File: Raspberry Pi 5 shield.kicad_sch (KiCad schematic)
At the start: 18 parts, among them J1 Raspberry Connector, J2 Conn_02x02_Odd_Even, U1 MCP2515-xSO

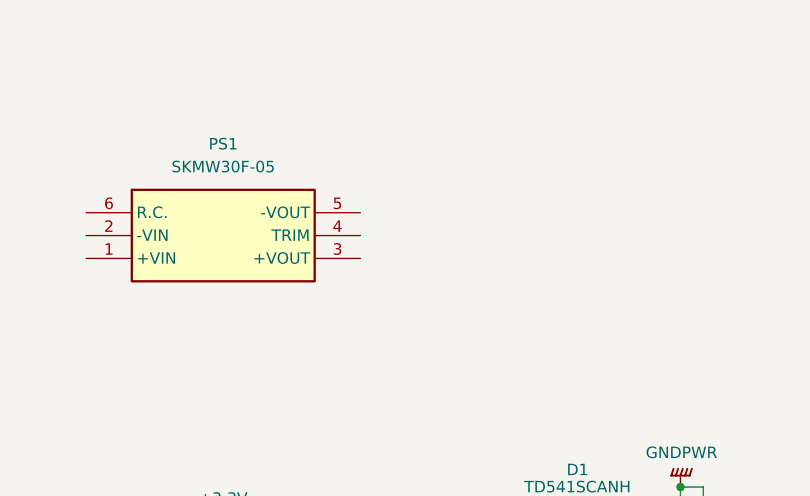
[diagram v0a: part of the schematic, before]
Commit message: Добавил подстроечный резистор к источнику питания
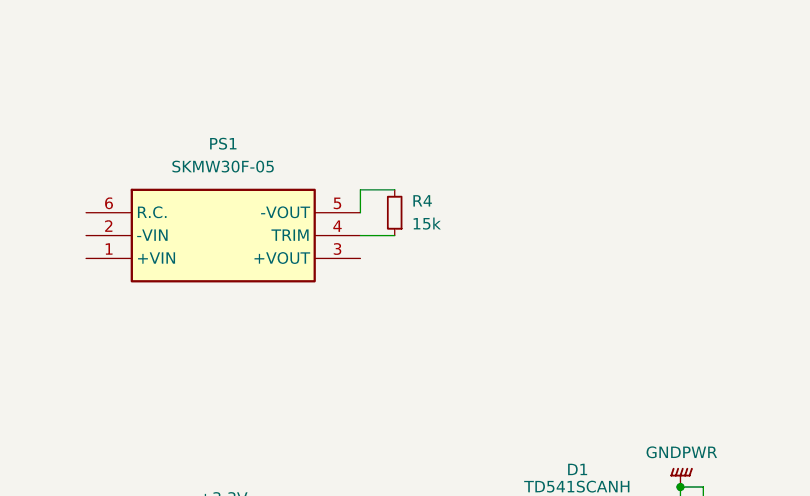
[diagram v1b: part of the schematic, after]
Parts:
- added R4: 15k, Resistor_SMD:R_0805_2012Metric_Pad1.20x1.40mm_HandSolder, symbol Device:R_Small
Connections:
- net at PS1.4 (TRIM): now also R4.1
- net at PS1.5 (-VOUT): now also R4.2
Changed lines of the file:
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@@
 	(wire
 		(pts
+			(xy 154.94 45.72) (xy 158.75 45.72)
+		)
+		(stroke
+			(width 0)
+			(type default)
+		)
+	)
+	(wire
+		(pts
 			(xy 189.23 85.09) (xy 202.565 85.09)
 		)
@@
 	(wire
 		(pts
+			(xy 154.94 40.64) (xy 158.75 40.64)
+		)
+		(stroke
+			(width 0)
+			(type default)
+		)
+	)
+	(wire
+		(pts
 			(xy 190.5 77.47) (xy 190.5 73.66)
 		)
@@
 	(wire
 		(pts
+			(xy 154.94 43.18) (xy 154.94 40.64)
+		)
+		(stroke
+			(width 0)
+			(type default)
+		)
+	)
+	(wire
+		(pts
 			(xy 154.94 85.09) (xy 168.91 85.09)
 		)
@@
 					(unit 1)
 				)
+			)
+		)
+	)
+	(symbol
+		(lib_id "Device:R_Small")
+		(at 158.75 43.18 180)
+		(unit 1)
+		(exclude_from_sim no)
+		(in_bom yes)
+		(on_board yes)
+		(dnp no)
+		(fields_autoplaced yes)
+		(property "Reference" "R4"
+			(at 160.655 41.91 0)
+			(effects
+				(font
+					(size 1.27 1.27)
+				)
+				(justify right)
+			)
+		)
+		(property "Value" "15k"
+			(at 160.655 44.45 0)
+			(effects
+				(font
+					(size 1.27 1.27)
+				)
+				(justify right)
+			)
+		)
+		(property "Footprint" "Resistor_SMD:R_0805_2012Metric_Pad1.20x1.40mm_HandSolder"
+			(at 158.75 43.18 0)
+			(effects
+				(font
+					(size 1.27 1.27)
+				)
+				(hide yes)
+			)
+		)
+		(property "Datasheet" "~"
+			(at 158.75 43.18 0)
+			(effects
+				(font
+					(size 1.27 1.27)
+				)
+				(hide yes)
+			)
+		)
+		(property "Description" "Resistor, small symbol"
+			(at 158.75 43.18 0)
+			(effects
+				(font
+					(size 1.27 1.27)
+				)
+				(hide yes)
+			)
+		)
+		(pin "2"
+		)
+		(pin "1"
+		)
+		(instances
+			(project "Raspberry Pi 5 shield"
+				(path "/2117c268-443a-419c-9380-190e5bd7137f"
+					(reference "R4")
+					(unit 1)
+				)

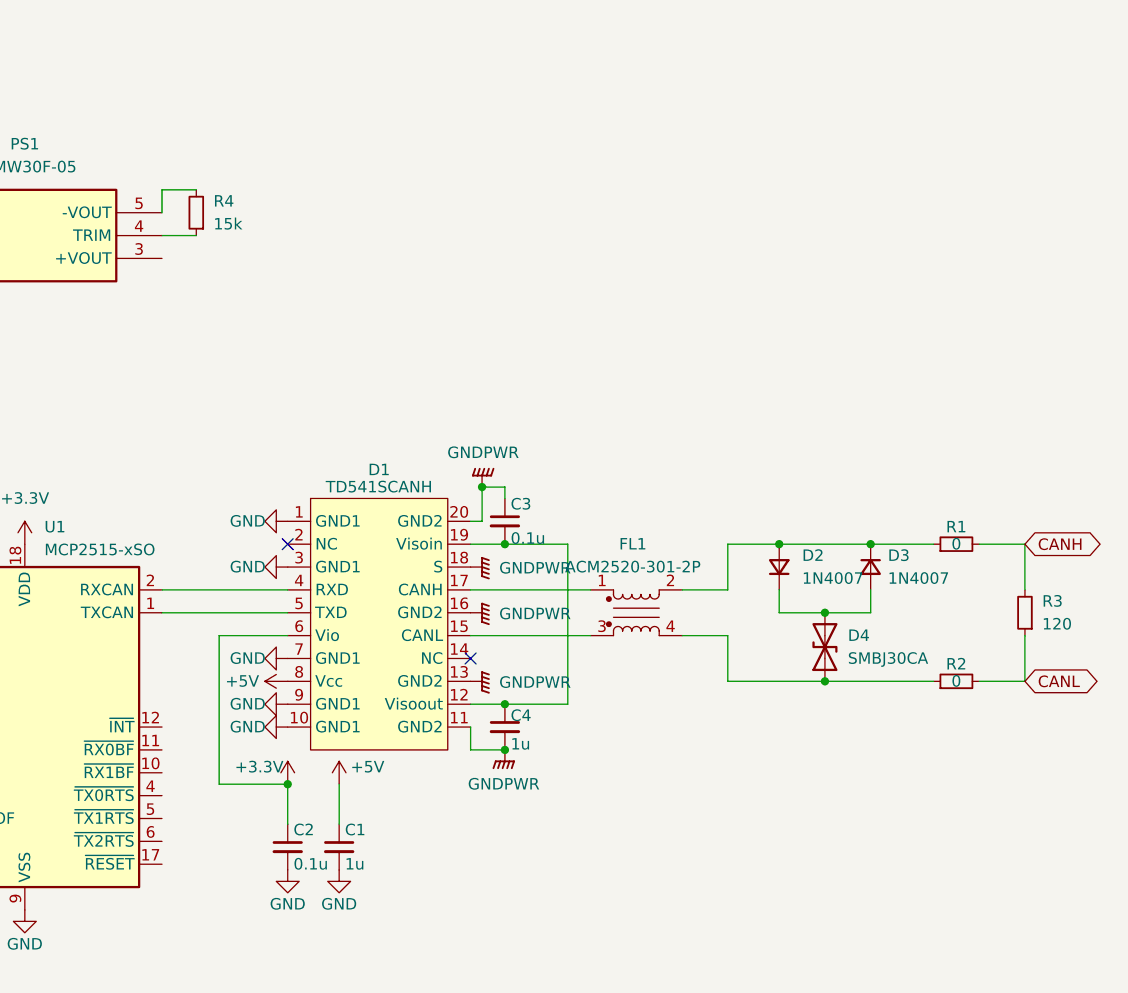
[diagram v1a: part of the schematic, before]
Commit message: Добавил конденсаторы по выходу
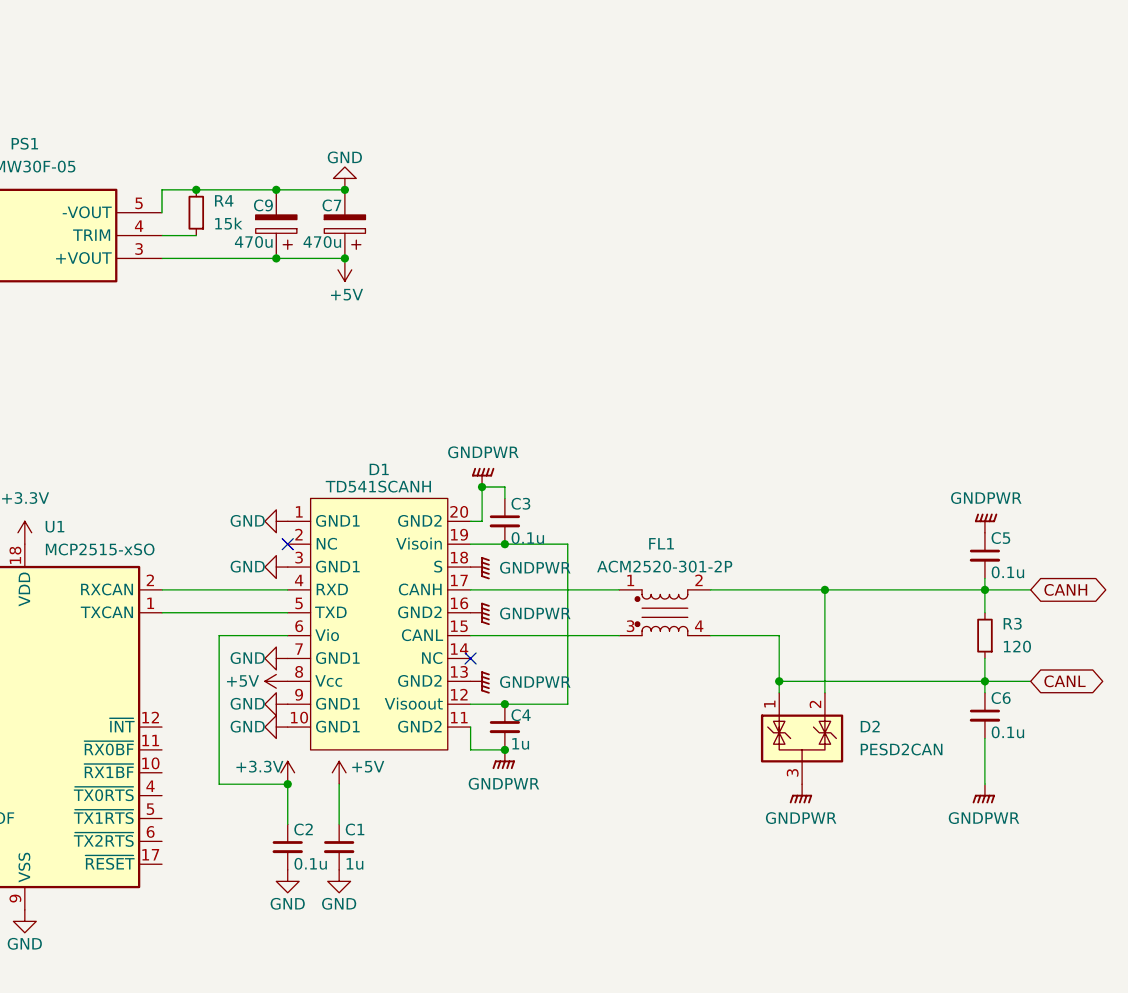
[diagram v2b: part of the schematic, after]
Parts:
- removed D2, D3: 1N4007, Diode_SMD:D_SMA_Handsoldering, symbol Device:D_Small
- removed D4: SMBJ30CA, Diode_SMD:D_SMB_Handsoldering, symbol Device:D_TVS
- removed R1, R2: 0, Resistor_SMD:R_0805_2012Metric_Pad1.20x1.40mm_HandSolder, symbol Device:R_Small
- added C5, C6: 0.1u, Capacitor_SMD:C_0805_2012Metric_Pad1.18x1.45mm_HandSolder, symbol Device:C_Small
- added C7, C9: 470u, Capacitor_SMD:CP_Elec_10x10, symbol Device:C_Polarized
- added D2: PESD2CAN, Package_TO_SOT_SMD:SOT-23, symbol Power_Protection:NUP2105L
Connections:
- net +5V: now also PS1.3 (+VOUT), C7.1, C9.1
- net CANH: now also FL1.2, C5.2, D2.2 (K)
- net CANL: now also FL1.4, C6.1, D2.1 (K)
- net GND: now also PS1.5 (-VOUT), R4.2, C7.2, C9.2
- net GNDPWR: now also C5.1, C6.2, D2.3 (A)
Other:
- moved on the sheet: FL1, R3

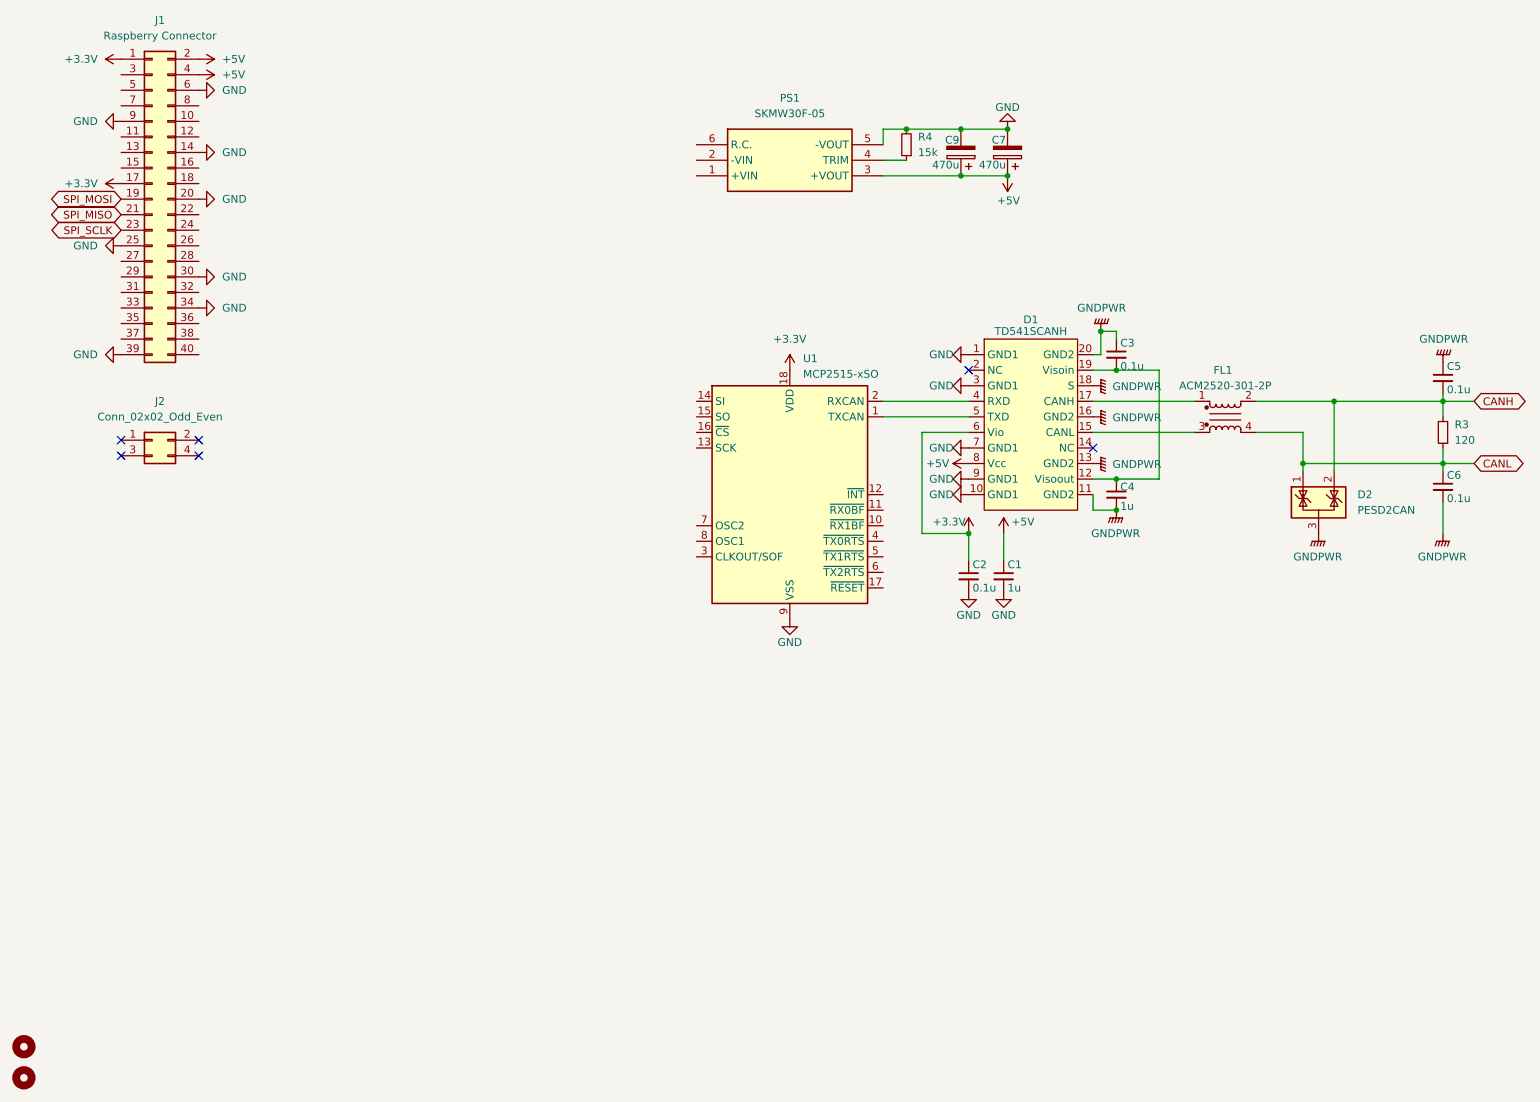
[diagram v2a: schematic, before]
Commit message: Добавил индикацию
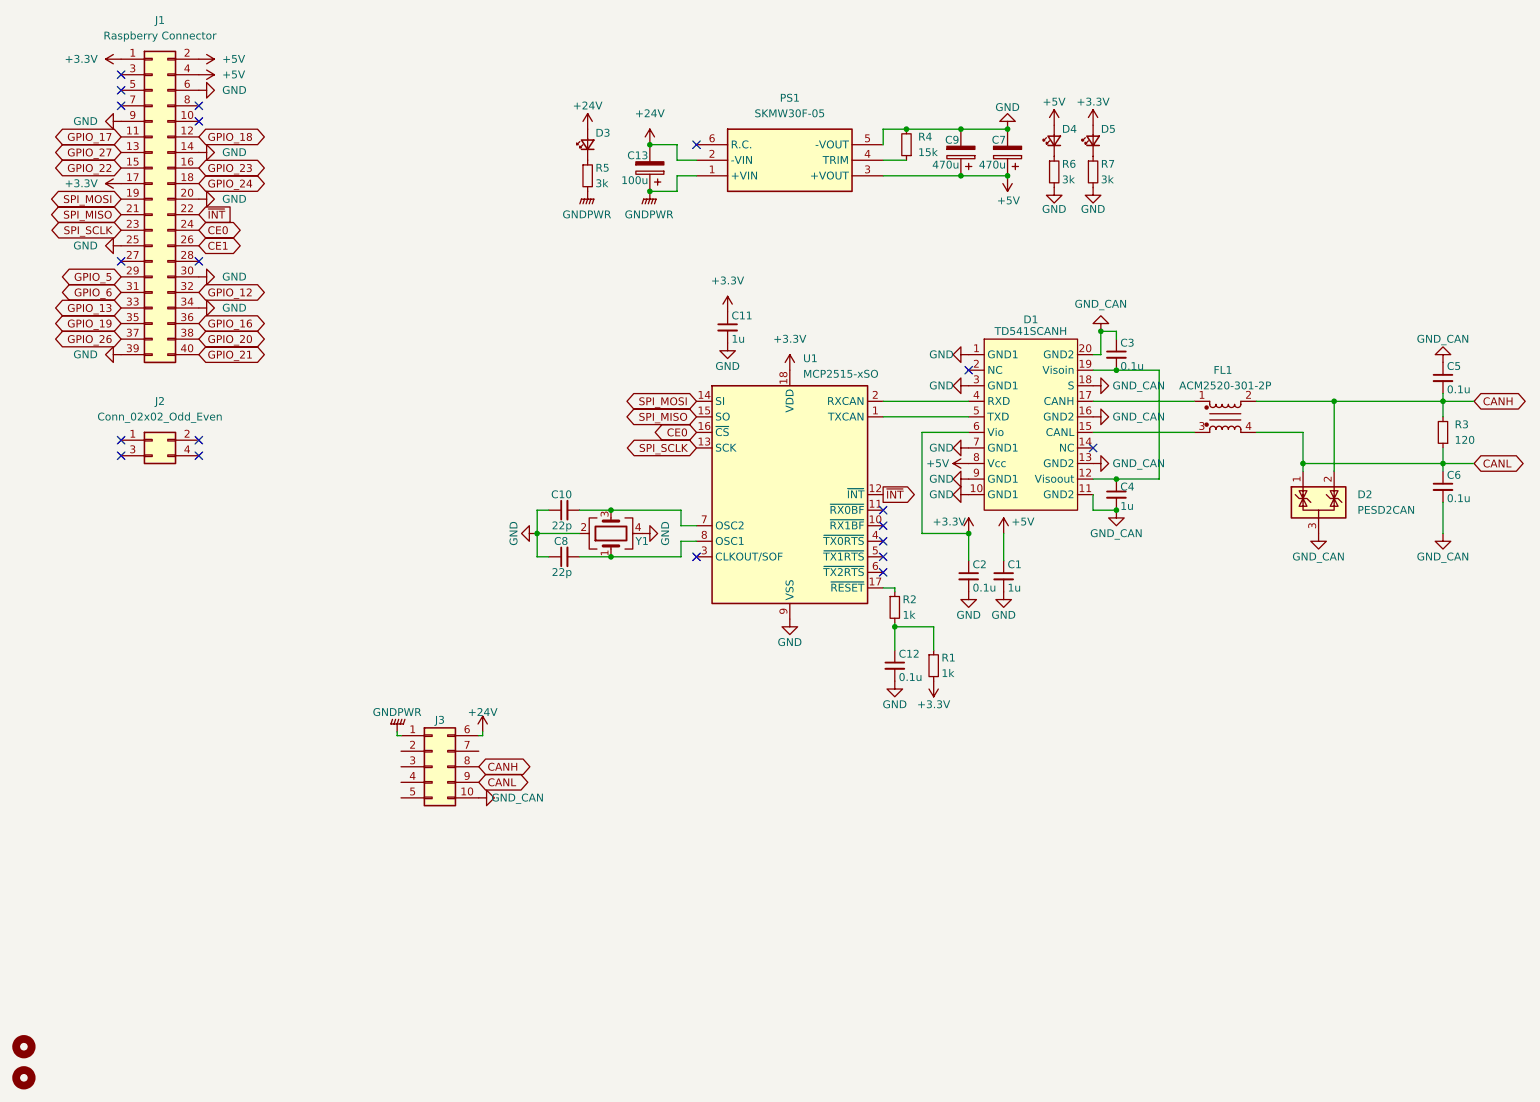
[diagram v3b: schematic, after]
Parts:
- added C10, C8: 22p, Capacitor_SMD:C_0805_2012Metric_Pad1.18x1.45mm_HandSolder, symbol Device:C_Small
- added C11: 1u, Capacitor_SMD:C_0805_2012Metric_Pad1.18x1.45mm_HandSolder, symbol Device:C_Small
- added C12: 0.1u, Capacitor_SMD:C_0805_2012Metric_Pad1.18x1.45mm_HandSolder, symbol Device:C_Small
- added C13: 100u, Capacitor_SMD:CP_Elec_10x10, symbol Device:C_Polarized
- added D3: PWR, LED_SMD:LED_0805_2012Metric_Pad1.15x1.40mm_HandSolder, symbol Device:LED_Small
- added D4, D5: LED_Small, LED_SMD:LED_0805_2012Metric_Pad1.15x1.40mm_HandSolder, symbol Device:LED_Small
- added J3: DS1073-01-2x5-MR3T6, Molex_My:MIni-Fit_02x05_Vertical, symbol Connector_Generic:Conn_02x05_Top_Bottom
- added R1, R2: 1k, Resistor_SMD:R_0805_2012Metric_Pad1.20x1.40mm_HandSolder, symbol Device:R_Small
- added R5, R6, R7: 3k, Resistor_SMD:R_0805_2012Metric_Pad1.20x1.40mm_HandSolder, symbol Device:R_Small
- added Y1: X322516MOB4SI, Crystal_My:X322516MOB4SI, symbol Device:Crystal_GND24
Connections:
- net +3.3V: now also C11.1, D5.2 (A), R1.2
- net +5V: now also D4.2 (A)
- net CANH: now also J3.8 (Pin_8)
- net CANL: now also J3.9 (Pin_9)
- net GND: now also C10.1, C11.2, C12.2, C8.1, R6.2, R7.2, Y1.2, Y1.4
- net GNDPWR: now also PS1.1 (+VIN), C13.1, J3.1 (Pin_1), R5.2; no longer C3.1, C4.2, C5.1, C6.2, D1.11 (GND2), D1.13 (GND2), D1.16 (GND2), D1.18 (S), D1.20 (GND2), D2.3 (A)
- net SPI_MISO: now also U1.15 (SO)
- net SPI_MOSI: now also U1.14 (SI)
- net SPI_SCLK: now also U1.13 (SCK)
- net ~{INT}: now reaches U1.12 (~{INT})
- net ~{INT}: now also J1.22 (Pin_22)
- net CE0: now reaches U1.16 (~{CS})
- net CE0: now also J1.24 (Pin_24)
- net at U1.17 (~{RESET}): now also R2.1
- net at U1.7 (OSC2): now also C10.2, Y1.3
- net at U1.8 (OSC1): now also C8.2, Y1.1
- net +24V: now reaches PS1.2 (-VIN)
- net +24V: now also C13.2, D3.2 (A), J3.6 (Pin_6)
- net GPIO_17: now reaches J1.11 (Pin_11)
- net GPIO_18: now reaches J1.12 (Pin_12)
- net GPIO_27: now reaches J1.13 (Pin_13)
- net GPIO_22: now reaches J1.15 (Pin_15)
- net GPIO_23: now reaches J1.16 (Pin_16)
- net GPIO_24: now reaches J1.18 (Pin_18)
- net CE1: now reaches J1.26 (Pin_26)
- net GPIO_5: now reaches J1.29 (Pin_29)
- net GPIO_6: now reaches J1.31 (Pin_31)
- net GPIO_12: now reaches J1.32 (Pin_32)
- net GPIO_13: now reaches J1.33 (Pin_33)
- net GPIO_19: now reaches J1.35 (Pin_35)
- net GPIO_16: now reaches J1.36 (Pin_36)
- net GPIO_26: now reaches J1.37 (Pin_37)
- net GPIO_20: now reaches J1.38 (Pin_38)
- net GPIO_21: now reaches J1.40 (Pin_40)
- new net: C12.1, R1.1, R2.2
- new net: D4.1 (K), R6.1
- new net: D3.1 (K), R5.1
- new net: D5.1 (K), R7.1
- new net GND_CAN: C3.1, C4.2, C5.1, C6.2, D1.11 (GND2), D1.13 (GND2), D1.16 (GND2), D1.18 (S), D1.20 (GND2), D2.3 (A), J3.10 (Pin_10)
- no-connect marks 6 -> 20

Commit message: Добавил BOM
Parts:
- C13: Name (none) -> EEHZA1H101P
- C7, C9: Name (none) -> B40900B5477M000
- D1: Name (none) -> TD541SCANH
- D2: Name (none) -> PESD2CAN
- FL1: Name (none) -> ACM2520-301-2P
- J1: Name (none) -> PBD-20 (DS1023-2x10)
- J2: Name (none) -> PBD-4 (DS1023-2X2)
- J3: value DS1073-01-2x5-MR3T6 -> DS1073-01-2x5-MVT6; Name (none) -> DS1073-01-2x5-MVT6
- PS1: Name (none) -> SKMW30F-05
- U1: Name (none) -> MCP2515-I/SO
- Y1: Name (none) -> X322516MOB4SI
